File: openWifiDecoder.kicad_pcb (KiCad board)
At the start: 4 copper layers, 16 x 23.6 mm, 63 parts, among them IC1 DRV8212DRLR, J1 Motor, J24 Hall, U1 MIC5317-1.8xM5, U2 MIC5219-3.3YM5, U3 ESP32-S3-MINI-1, U4 ICM-20948, U5 LTC4054ES5-4.2, U6 TL331, U7 BQ27441DRZT-G1A

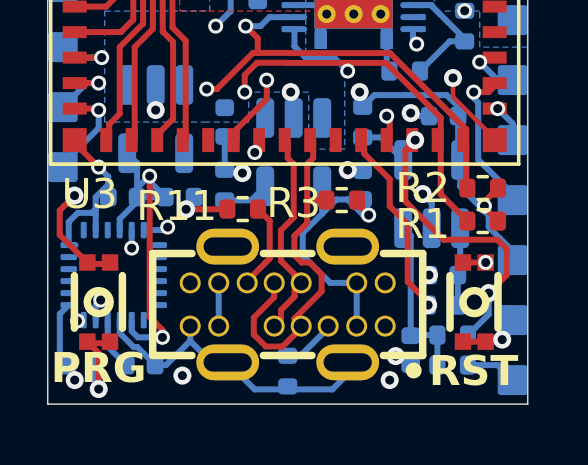
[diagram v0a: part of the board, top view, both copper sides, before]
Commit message: add EN PullUp
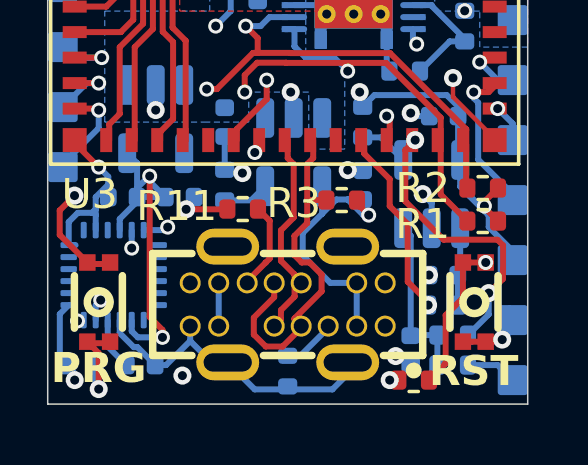
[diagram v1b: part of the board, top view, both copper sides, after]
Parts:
- added R14: 10k, Resistor_SMD:R_0402_1005Metric, F.Cu at (106.7, 86.8)
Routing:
- net Net-(U3-EN): track 18.6 -> 23.0 mm
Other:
- board text added: "1.1"
- board text removed: "1.0"

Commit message: finished Layout, started PCB design agound ESP32
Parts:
- added C16: 10u, Capacitor_SMD:C_0805_2012Metric, F.Cu at (113.9, 81.4)
- added C17: 10u X7R, Capacitor_SMD:C_0805_2012Metric, F.Cu at (113.9, 84.4)
- added C18: 1uF X7R, Capacitor_SMD:C_0402_1005Metric, F.Cu at (172.2, 73.8)
- added C19: 10u X7R, Capacitor_SMD:C_0805_2012Metric, F.Cu at (186.1, 91.9)
- added C20: .1uF X7R, Capacitor_SMD:C_0402_1005Metric, F.Cu at (176.1, 101.6)
- added C21: .1uF X7R, Capacitor_SMD:C_0402_1005Metric, F.Cu at (178.9, 97.6)
- added C22: .1uF X7R, Capacitor_SMD:C_0402_1005Metric, F.Cu at (161.2, 77.6)
- added C23: TBCC, Capacitor_SMD:C_0805_2012Metric, F.Cu at (166.9, 66.1)
- added C24: C, Capacitor_SMD:C_0402_1005Metric, F.Cu at (157.1, 67.0)
- added C25: C, Capacitor_SMD:C_0402_1005Metric, F.Cu at (157.0, 64.0)
- added C26: C, Capacitor_SMD:C_0402_1005Metric, F.Cu at (125.3, 83.2)
- added C27: C, Capacitor_SMD:C_0402_1005Metric, F.Cu at (125.3, 85.2)
- added L1: 1.5u 1.5A, Inductor_SMD:L_1008_2520Metric, F.Cu at (107.6, 72.9)
- added L2: 2n, Inductor_SMD:L_0402_1005Metric, F.Cu at (189.8, 88.4)
- added L3: 24n, Inductor_SMD:L_0402_1005Metric, F.Cu at (161.5, 66.7)
- added L4: L, Inductor_SMD:L_0402_1005Metric, F.Cu at (157.6, 65.5)
- added L5: L, Inductor_SMD:L_0402_1005Metric, F.Cu at (133.3, 78.0)
- added R15: 100k, Resistor_SMD:R_0603_1608Metric, F.Cu at (113.7, 87.2)
- added U8: W25Q16JVUUIQ, EasyEda:USON-8_L4.0-W3.0-P0.80-BL_AT25SL321, F.Cu at (164.0, 77.2)
- added U9: RFANT3216120A5T, EasyEda:FILTER-SMD_1206-2P-L3.2-W1.6-L, F.Cu at (159.1, 60.5)
- added Y1: 40MHz 10pF, Crystal:Crystal_SMD_2016-4Pin_2.0x1.6mm, F.Cu at (164.2, 66.0)
- BAT1, C1, C10, C11, C12, C13, C14, C15, C3, C4, C6, C7, C8, C9, IC1, IO1, IO10, IO11, IO12, IO13, IO14, IO15, IO16, IO17, IO18, IO19, IO2, IO3, IO4, IO5, IO6, IO7, IO8, IO9, J1, J24, R10, R12, R13, R4, R5, R6, R7, R8, R9, RX0, TX0, U1, U4, U5, U6, U7: moved to F.Cu
- C2: value 22uF X7R -> TBC; moved to F.Cu
- C5: value 1uF X7R -> 10u X7R; footprint Capacitor_SMD:C_0402_1005Metric -> Capacitor_SMD:C_0805_2012Metric; moved to F.Cu
- U2: value MIC5219-3.3YM5 -> TPS63051RMWR; footprint Package_TO_SOT_SMD:SOT-23-5 -> EasyEda:QFN-12_L2.5-W2.5-P0.50-TL; moved to F.Cu
- U3: value ESP32-S3-MINI-1 -> ESP32-S3; footprint RF_Module:ESP32-S2-MINI-1 -> Package_DFN_QFN:QFN-56-1EP_7x7mm_P0.4mm_EP4x4mm_ThermalVias
- moved C1 76.8 mm to (174.6, 83.5)
- moved C2 65.0 mm to (164.2, 68.8)
- moved U3 56.8 mm to (159.1, 72.3), turned to -45 degrees
- moved U2 30.1 mm to (115.3, 97.8), turned to 0 degrees
- moved C6 28.1 mm to (91.2, 91.8)
- moved J1 24.0 mm to (108.5, 93.8), turned to 0 degrees
- moved C10 23.8 mm to (94.1, 91.8), turned to 0 degrees
- moved IO12 23.4 mm to (101.5, 87.9), turned to 0 degrees
- moved IC1 22.8 mm to (112.2, 92.3)
- moved IO11 21.4 mm to (101.5, 85.9), turned to 0 degrees
- moved R5 20.3 mm to (91.2, 85.8), turned to 0 degrees
- moved R4 20.1 mm to (91.2, 83.9), turned to 0 degrees
- moved FLASH1 19.9 mm to (112.2, 72.4), turned to 0 degrees
- moved IO10 19.6 mm to (101.5, 83.9), turned to 0 degrees
- moved IO6 18.7 mm to (99.5, 87.9), turned to 0 degrees
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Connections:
- C1 pad 1: +3V3 -> Net-(C1-Pad1)
- C13 pad 2: +3V3 -> VDD_SPI
- C2 pad 1: +3V3 -> Net-(C2-Pad1)
- C5 pad 1: +3V3 -> VDD_SPI
- C8 pad 2: +3V3 -> VDD_SPI
- FLASH1 pad 3: Net-(U3-IO0) -> Net-(FLASH1-Pad3)
- FLASH1 pad 4: Net-(U3-IO0) -> Net-(FLASH1-Pad3)
- IO1 pad 1: Net-(IO1-Pin_1) -> unconnected-(IO1-Pin_1-Pad1)
- IO10 pad 1: Net-(IO10-Pin_1) -> unconnected-(IO10-Pin_1-Pad1)
- IO11 pad 1: Net-(IO11-Pin_1) -> unconnected-(IO11-Pin_1-Pad1)
- IO12 pad 1: Net-(IO12-Pin_1) -> unconnected-(IO12-Pin_1-Pad1)
- IO13 pad 1: Net-(IO13-Pin_1) -> unconnected-(IO13-Pin_1-Pad1)
- IO14 pad 1: Net-(IO14-Pin_1) -> unconnected-(IO14-Pin_1-Pad1)
- IO15 pad 1: Net-(IO15-Pin_1) -> unconnected-(IO15-Pin_1-Pad1)
- IO16 pad 1: Net-(IO16-Pin_1) -> unconnected-(IO16-Pin_1-Pad1)
- IO17 pad 1: Net-(IO17-Pin_1) -> unconnected-(IO17-Pin_1-Pad1)
- IO18 pad 1: Net-(IO18-Pin_1) -> unconnected-(IO18-Pin_1-Pad1)
- IO19 pad 1: Net-(IO19-Pin_1) -> unconnected-(IO19-Pin_1-Pad1)
- IO2 pad 1: Net-(IO2-Pin_1) -> unconnected-(IO2-Pin_1-Pad1)
- IO3 pad 1: Net-(IO3-Pin_1) -> unconnected-(IO3-Pin_1-Pad1)
- IO4 pad 1: Net-(IO4-Pin_1) -> unconnected-(IO4-Pin_1-Pad1)
- IO5 pad 1: Net-(IO5-Pin_1) -> unconnected-(IO5-Pin_1-Pad1)
- IO6 pad 1: Net-(IO6-Pin_1) -> unconnected-(IO6-Pin_1-Pad1)
- IO7 pad 1: Net-(IO7-Pin_1) -> unconnected-(IO7-Pin_1-Pad1)
- IO8 pad 1: Net-(IO8-Pin_1) -> unconnected-(IO8-Pin_1-Pad1)
- IO9 pad 1: Net-(IO9-Pin_1) -> unconnected-(IO9-Pin_1-Pad1)
- J24 pad 1: +3V3 -> VDD_SPI
- R1 pad 1: +3V3 -> VDD_SPI
- R10 pad 2: +3V3 -> VDD_SPI
- R14 pad 1: Net-(U3-EN) -> Net-(R14-Pad1)
- R14 pad 2: +3V3 -> VDD_SPI
- R2 pad 1: +3V3 -> VDD_SPI
- RESET1 pad 3: Net-(U3-EN) -> Net-(R14-Pad1)
- RESET1 pad 4: Net-(U3-EN) -> Net-(R14-Pad1)
- U2 pad 1: +BATT -> Net-(U2-L1)
- U2 pad 3: +BATT -> Net-(U2-L2)
- U2 pad 4: unconnected-(U2-BP-Pad4) -> VDD_SPI
- U2 pad 5: +3V3 -> VDD_SPI
- U3 pad 1: GND -> Net-(U3-LNA_IN)
- U3 pad 10: Net-(IO4-Pin_1) -> /ESP/GPIO5
- U3 pad 11: Net-(IO9-Pin_1) -> /ESP/GPIO6
- U3 pad 12: Net-(IO10-Pin_1) -> /ESP/GPIO7
- U3 pad 13: Net-(IO3-Pin_1) -> /ESP/GPIO8
- U3 pad 14: Net-(IO2-Pin_1) -> /ESP/GPIO9
- U3 pad 15: Net-(IO1-Pin_1) -> /ESP/GPIO10
- U3 pad 16: Net-(IO11-Pin_1) -> /ESP/GPIO11
- U3 pad 17: Net-(IO12-Pin_1) -> /ESP/GPIO12
- U3 pad 18: Net-(IO13-Pin_1) -> /ESP/GPIO13
- U3 pad 19: Net-(IO14-Pin_1) -> /ESP/GPIO14
- U3 pad 2: GND -> Net-(L2-Pad2)
- U3 pad 20: unconnected-(U3-IO16-Pad20) -> VDD_SPI
- U3 pad 21: IMU_INT -> unconnected-(U3-XTAL_32K_P-Pad21)
- U3 pad 22: FSYNC -> unconnected-(U3-XTAL_32K_N-Pad22)
- U3 pad 23: D- -> /ESP/GPIO17
- U3 pad 24: D+ -> /ESP/GPIO18
- U3 pad 25: unconnected-(U3-IO21-Pad25) -> /ESP/GPIO19
- U3 pad 26: COMP_DAC -> /ESP/GPIO20
- U3 pad 27: GAUGE_INT -> /ESP/GPIO21
- U3 pad 28: DIG_HALL -> unconnected-(U3-SPICS1-Pad28)
- U3 pad 29: SDA -> VDD_SPI
- U3 pad 3: +3V3 -> Net-(L2-Pad2)
- U3 pad 30: SCL -> HOLD
- U3 pad 31: Net-(IO18-Pin_1) -> WP
- U3 pad 32: Net-(IO19-Pin_1) -> CS
- U3 pad 33: Net-(IO17-Pin_1) -> CLK
- U3 pad 34: unconnected-(U3-IO38-Pad34) -> SDO
- U3 pad 35: unconnected-(U3-IO39-Pad35) -> SDI
- U3 pad 36: Net-(IO16-Pin_1) -> unconnected-(U3-SPICLK_N-Pad36)
- U3 pad 37: MPWM1 -> unconnected-(U3-SPICLK_P-Pad37)
- U3 pad 38: MPWM2 -> /ESP/GPIO33
- U3 pad 39: TX -> /ESP/GPIO34
- U3 pad 4: Net-(U3-IO0) -> VDD_SPI
- U3 pad 40: RX -> /ESP/GPIO35
- U3 pad 41: Net-(IO15-Pin_1) -> /ESP/GPIO36
- U3 pad 42: GND -> /ESP/GPIO37
- U3 pad 43: GND -> /ESP/GPIO38
- U3 pad 45: Net-(U3-EN) -> unconnected-(U3-MTDO-Pad45)
- U3 pad 46: GND -> VDD_SPI
- U3 pad 47: GND -> unconnected-(U3-MTDI-Pad47)
- U3 pad 48: GND -> unconnected-(U3-MTMS-Pad48)
- U3 pad 49: GND -> unconnected-(U3-U0TXD-Pad49)
- U3 pad 5: Net-(IO8-Pin_1) -> /ESP/GPIO0
- U3 pad 50: GND -> unconnected-(U3-U0RXD-Pad50)
- U3 pad 51: GND -> unconnected-(U3-GPIO45-Pad51)
- U3 pad 52: GND -> unconnected-(U3-GPIO46-Pad52)
- U3 pad 53: GND -> Net-(U3-XTAL_N)
- U3 pad 54: GND -> Net-(U3-XTAL_P)
- U3 pad 55: GND -> VDD_SPI
- U3 pad 56: GND -> VDD_SPI
- U3 pad 6: Net-(IO7-Pin_1) -> /ESP/GPIO1
- U3 pad 7: Net-(IO6-Pin_1) -> /ESP/GPIO2
- U3 pad 8: Net-(IO5-Pin_1) -> /ESP/GPIO3
- U3 pad 9: unconnected-(U3-IO5-Pad9) -> /ESP/GPIO4
- U4 pad 13: +3V3 -> VDD_SPI
- U6 pad 5: +3V3 -> VDD_SPI
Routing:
- net GND: track 35.6 -> 0.00 mm, vias 31 -> 0
- net +3V3: track 33.6 -> 0.00 mm, vias 8 -> 0
- net Net-(U3-EN): track 23.0 -> 0.00 mm, vias 2 -> 0
- net SCL: track 21.5 -> 0.00 mm, vias 3 -> 0
- net SDA: track 21.3 -> 0.00 mm, vias 3 -> 0
- net Net-(IO14-Pin_1): track 20.0 -> 0.00 mm, vias 1 -> 0
- net Net-(IO13-Pin_1): track 18.7 -> 0.00 mm, vias 1 -> 0
- net Net-(IO11-Pin_1): track 17.9 -> 0.00 mm, vias 1 -> 0
- net Net-(IO12-Pin_1): track 17.9 -> 0.00 mm, vias 1 -> 0
- net Net-(U3-IO0): track 16.8 -> 0.00 mm, vias 2 -> 0
- net +5V: track 16.2 -> 0.00 mm, vias 1 -> 0
- net IMU_INT: track 15.8 -> 0.00 mm, vias 2 -> 0
- net Net-(BAT1-Pin_2): track 14.2 -> 0.00 mm, vias 2 -> 0
- net Net-(IO16-Pin_1): track 14.2 -> 0.00 mm, vias 1 -> 0
- net Net-(IO10-Pin_1): track 12.8 -> 0.00 mm, vias 1 -> 0
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- removed copper zone on In1.Cu, net +3V3
- removed copper zone on B.Cu, net +BATT
- removed copper zone on F.Cu, net GND
- removed copper zone on In2.Cu, net GND
- removed copper zone on B.Cu, net Net-(BAT1-Pin_2)
- removed copper zone on B.Cu, net Net-(IC1-OUT1)
- removed copper zone on B.Cu, net Net-(IC1-OUT2)
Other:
- board outline removed
- board text removed: "+"
- board text removed: "-"
- board text removed: "1"
- board text removed: "1.1"
- board text removed: "10"
- board text removed: "11"
- board text removed: "12"
- board text removed: "13"
- board text removed: "14"
- board text removed: "15"
- board text removed: "16"
- board text removed: "17"
- board text removed: "18"
- board text removed: "19"
- board text removed: "2"
- board text removed: "3"
- board text removed: "4"
- board text removed: "5"
- board text removed: "6"
- board text removed: "7"
- board text removed: "8"
- board text removed: "9"
- board text removed: "BAT"
- board text removed: "HALL"
- board text removed: "Motor"
- board text removed: "PRG"
- board text removed: "R"
- board text removed: "RST"
- board text removed: "T"
- board text removed: "der Graph"
- board text removed: "openWiFi decoder"

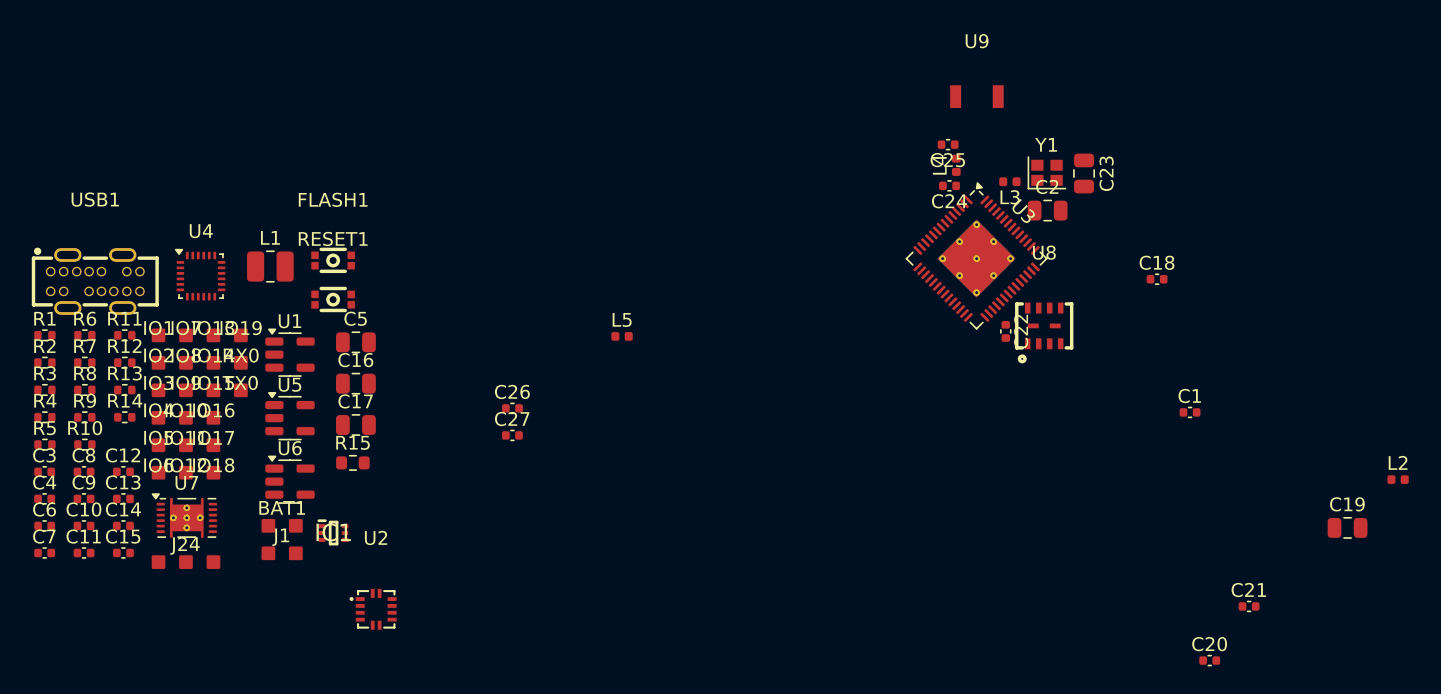
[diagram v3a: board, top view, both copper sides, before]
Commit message: pcb parts placed not connected
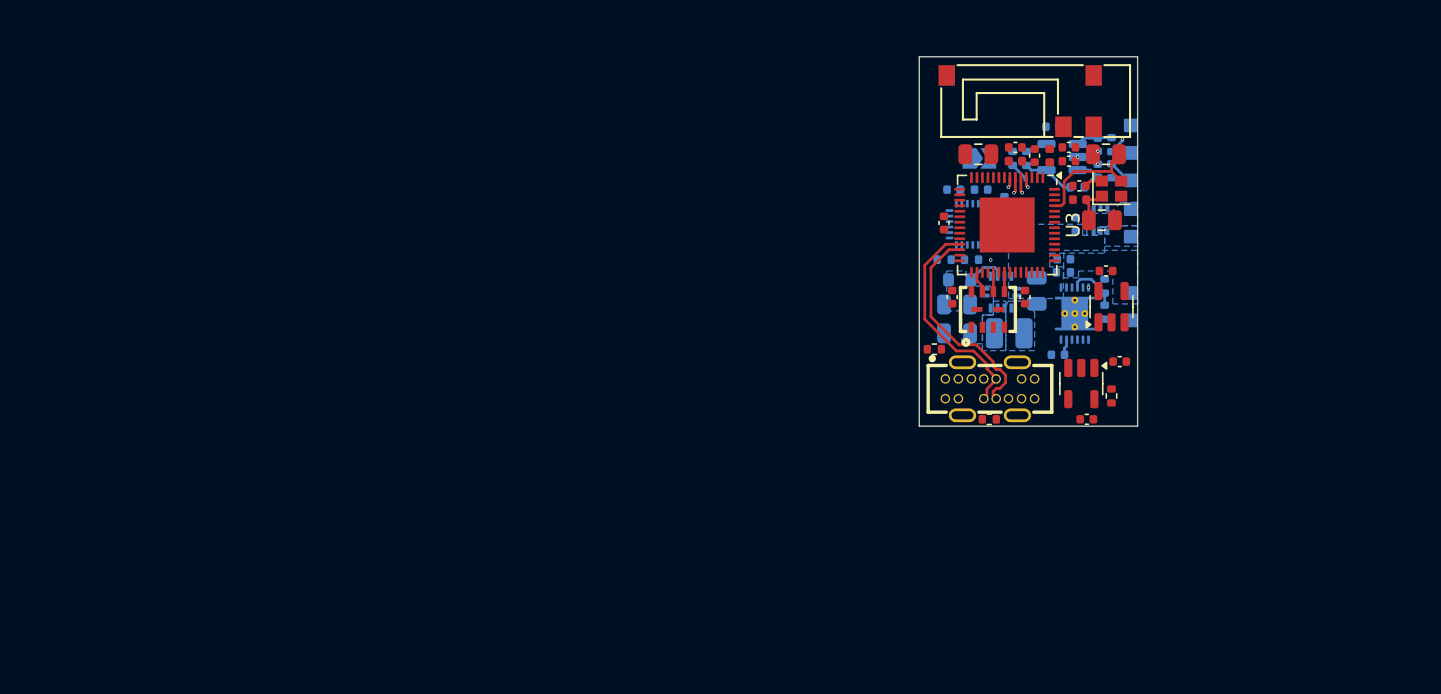
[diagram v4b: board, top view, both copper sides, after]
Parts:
- removed C27: C, Capacitor_SMD:C_0402_1005Metric
- removed FLASH1: FLASH, easyeda2kicad:SW-SMD_4P-L2.6-W1.6-P0.75-LS3.0
- removed IO1, IO8: 1, padLib:SolderPad_1mm_1Pin
- removed IO10, IO11, IO12, IO13, IO14, IO15, IO16, IO17, IO18, IO19, IO4, IO5, IO6, IO9, RX0, TX0: Conn_01x01_Socket, padLib:SolderPad_1mm_1Pin
- removed IO2, IO7: 2, padLib:SolderPad_1mm_1Pin
- removed IO3: 3, padLib:SolderPad_1mm_1Pin
- removed L5: L, Inductor_SMD:L_0402_1005Metric
- removed R3: USB_PU, Resistor_SMD:R_0402_1005Metric
- removed RESET1: RESET, easyeda2kicad:SW-SMD_4P-L2.6-W1.6-P0.75-LS3.0
- removed U9: RFANT3216120A5T, EasyEda:FILTER-SMD_1206-2P-L3.2-W1.6-L
- added ANT1: PRO-OB-440, EasyEda:ANT-SMD_5P-L13.8-W5.2_PRO-OB-440, F.Cu at (162.2, 60.8)
- added JP1: Download Mode, padLib:SolderJumper-2_P1.3mm_Open_TrianglePad1.0x1.5mm_SMALLER, B.Cu at (159.3, 65.0)
- BAT1, C10, C11, C13, C14, C15, C16, C17, C5, C6, C7, C8, C9, IC1, J1, J24, L1, R1, R10, R12, R13, R14, R15, R2, R4, R5, R6, R8, U2, U4, U6, U7: moved to B.Cu
- C26: value C -> 1uF X7R
- U3: footprint Package_DFN_QFN:QFN-56-1EP_7x7mm_P0.4mm_EP4x4mm_ThermalVias -> Package_DFN_QFN:QFN-56-1EP_7x7mm_P0.4mm_EP4x4mm
- moved C4 79.1 mm to (168.5, 73.2)
- moved C3 78.7 mm to (169.5, 79.8), turned to 180 degrees
- moved C6 78.2 mm to (166.3, 69.8), turned to -90 degrees
- moved R5 77.8 mm to (168.4, 76.2), turned to 90 degrees
- moved C15 76.9 mm to (167.9, 64.0), turned to -90 degrees
- moved C14 75.5 mm to (167.9, 65.9), turned to -90 degrees
- moved J24 75.0 mm to (170.3, 64.6), turned to -90 degrees
- moved R4 74.9 mm to (165.4, 73.3), turned to 180 degrees
- moved R7 74.8 mm to (168.9, 82.3), turned to -90 degrees
- moved R6 74.4 mm to (168.4, 74.3), turned to 90 degrees
- moved R13 74.0 mm to (168.9, 64.0), turned to 90 degrees
- moved C10 73.9 mm to (165.4, 72.3), turned to 180 degrees
- moved R8 73.8 mm to (166.4, 67.1), turned to 180 degrees
- moved R12 73.2 mm to (168.9, 65.9), turned to 90 degrees
- moved C13 72.9 mm to (164.6, 62.7), turned to 180 degrees
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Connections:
- net /ESP/GPIO3 renamed /ESP/GPIO3 JTAG Source
- C1 pad 1: Net-(C1-Pad1) -> +3V3
- C13 pad 2: VDD_SPI -> +3V3
- C16 pad 1: VDD_SPI -> +3V3
- C19 pad 1: VDD_SPI -> +3V3
- C20 pad 2: VDD_SPI -> +3V3
- C21 pad 2: VDD_SPI -> +3V3
- C22 pad 1: VDD_SPI -> Net-(U3-VDD3P3_CPU)
- C25 pad 1: Net-(C25-Pad1) -> Net-(ANT1-FEED)
- C26 pad 1: Net-(C25-Pad1) -> GND
- C26 pad 2: GND -> Net-(C26-Pad2)
- C3 pad 1: +BATT -> +3V3
- C5 pad 1: VDD_SPI -> +3V3
- C8 pad 2: VDD_SPI -> +3V3
- J24 pad 1: VDD_SPI -> +3V3
- L2 pad 1: Net-(C1-Pad1) -> +3V3
- L2 pad 2: Net-(L2-Pad2) -> Net-(C26-Pad2)
- L4 pad 2: Net-(C25-Pad1) -> Net-(ANT1-FEED)
- R1 pad 1: VDD_SPI -> +3V3
- R10 pad 2: VDD_SPI -> +3V3
- R14 pad 1: Net-(R14-Pad1) -> /ESP/RST
- R14 pad 2: VDD_SPI -> +3V3
- R15 pad 1: VDD_SPI -> +3V3
- R2 pad 1: VDD_SPI -> +3V3
- U1 pad 1: +BATT -> +3V3
- U1 pad 3: +BATT -> +3V3
- U2 pad 4: VDD_SPI -> +3V3
- U2 pad 5: VDD_SPI -> +3V3
- U3 pad 10: /ESP/GPIO5 -> MPWM1
- U3 pad 11: /ESP/GPIO6 -> IMU_INT
- U3 pad 2: Net-(L2-Pad2) -> Net-(C26-Pad2)
- U3 pad 20: VDD_SPI -> +3V3
- U3 pad 23: /ESP/GPIO17 -> SCL
- U3 pad 24: /ESP/GPIO18 -> SDA
- U3 pad 25: /ESP/GPIO19 -> D-
- U3 pad 26: /ESP/GPIO20 -> D+
- U3 pad 27: /ESP/GPIO21 -> FSYNC
- U3 pad 3: Net-(L2-Pad2) -> Net-(C26-Pad2)
- U3 pad 4: VDD_SPI -> /ESP/RST
- U3 pad 42: /ESP/GPIO37 -> GAUGE_INT
- U3 pad 46: VDD_SPI -> Net-(U3-VDD3P3_CPU)
- U3 pad 5: /ESP/GPIO0 -> /ESP/GPIO0 Flash Mode
- U3 pad 51: unconnected-(U3-GPIO45-Pad51) -> GND
- U3 pad 52: unconnected-(U3-GPIO46-Pad52) -> GND
- U3 pad 55: VDD_SPI -> +3V3
- U3 pad 56: VDD_SPI -> +3V3
- U3 pad 6: /ESP/GPIO1 -> COMP_DAC
- U3 pad 7: /ESP/GPIO2 -> DIG_HALL
- U3 pad 9: /ESP/GPIO4 -> MPWM2
- U4 pad 13: VDD_SPI -> +3V3
- U6 pad 5: VDD_SPI -> +3V3
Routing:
- net D-: track 0.00 -> 16.0 mm
- net D+: track 0.00 -> 15.9 mm
- net Net-(U3-XTAL_N): track 0.00 -> 8.57 mm
- net DIG_HALL: track 0.00 -> 4.60 mm, vias 0 -> 1
- net Net-(U6-+): track 0.00 -> 3.98 mm
- net Net-(U7-BIN): track 0.00 -> 3.77 mm
- net Net-(C2-Pad1): track 0.00 -> 2.97 mm
- net Net-(U2-PG): track 0.00 -> 2.81 mm
- net Net-(U6--): track 0.00 -> 2.65 mm
- net COMP_DAC: track 0.00 -> 2.38 mm, vias 0 -> 2
- net /ESP/RST: track 0.00 -> 2.19 mm, vias 0 -> 1
- net Net-(J24-Pin_3): track 0.00 -> 1.90 mm
- net HOLD: track 0.00 -> 1.57 mm
- net SDI: track 0.00 -> 1.40 mm
- net CLK: track 0.00 -> 1.40 mm
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- added copper zone on B.Cu, net +3V3
- added copper zone on B.Cu, net +BATT
- added copper zone on B.Cu, net Net-(BAT1-Pin_2)
- added copper zone on B.Cu, net Net-(IC1-OUT1)
- added copper zone on B.Cu, net Net-(IC1-OUT2)
- added copper zone on B.Cu, net Net-(U2-L1)
- added copper zone on B.Cu, net Net-(U2-L2)
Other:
- board outline added: 15.9 x 26.9 mm

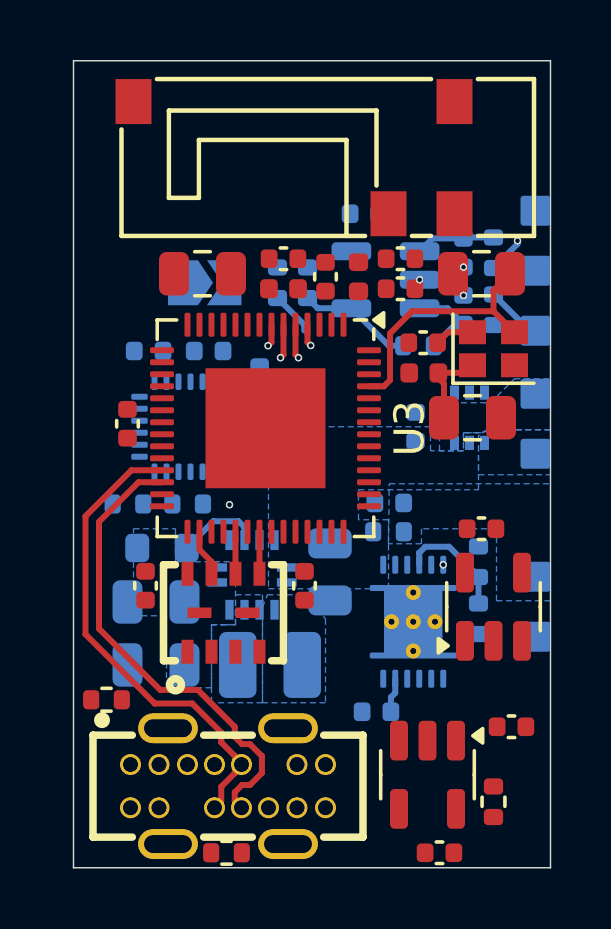
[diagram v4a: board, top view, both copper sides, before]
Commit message: pcb complete, drc failing 133 Errors
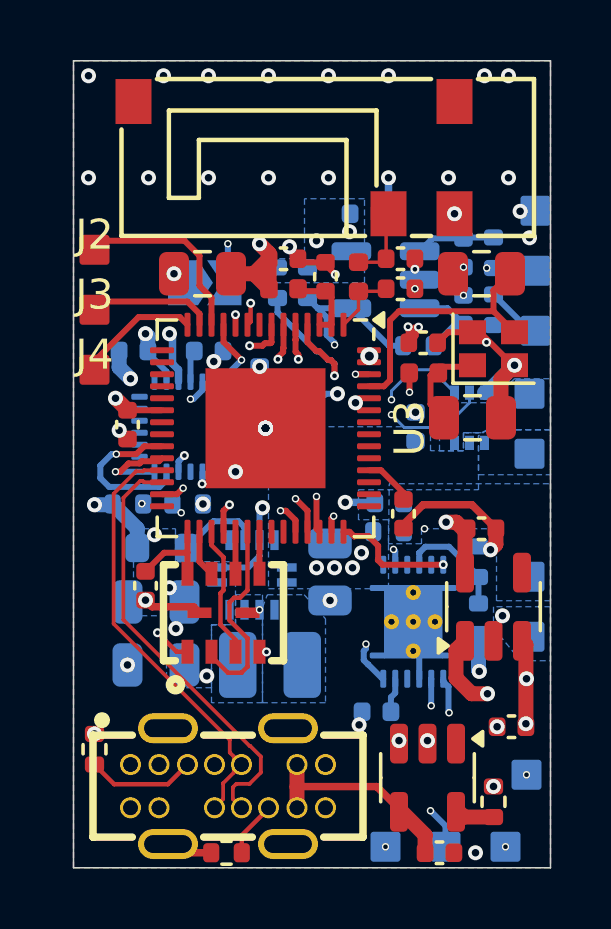
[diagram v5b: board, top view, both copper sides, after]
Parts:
- added J2: Conn_01x01_Pin, padLib:SolderPad_1mm_1Pin, F.Cu at (155.6, 63.9)
- added J3: Conn_01x01_Pin, padLib:SolderPad_1mm_1Pin, F.Cu at (155.6, 65.9)
- added J4: Conn_01x01_Pin, padLib:SolderPad_1mm_1Pin, F.Cu at (155.6, 67.9)
- added J5: Conn_01x01_Pin, padLib:SolderPad_1mm_1Pin, B.Cu at (165.3, 83.8)
- added J6: Conn_01x01_Pin, padLib:SolderPad_1mm_1Pin, B.Cu at (167.3, 83.8)
- added J7: Conn_01x01_Pin, padLib:SolderPad_1mm_1Pin, B.Cu at (169.3, 83.8)
- added J8: Conn_01x01_Pin, padLib:SolderPad_1mm_1Pin, B.Cu at (170.0, 81.4)
- moved C22 4.08 mm to (165.9, 72.7)
- moved R9 1.70 mm to (155.6, 80.5), turned to 90 degrees
- moved C7 0.50 mm to (156.9, 67.3)
- moved BAT1 0.20 mm to (170.1, 75.8)
- moved J1 0.20 mm to (170.1, 69.7)
- moved U5 0.10 mm to (166.7, 81.5)
- turned R11 to 180 degrees
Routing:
- net GND: track 1.31 -> 26.5 mm, vias 3 -> 56
- net SCL: track 0.00 -> 20.7 mm, vias 0 -> 3
- net SDA: track 0.00 -> 19.5 mm, vias 0 -> 3
- net +3V3: track 0.00 -> 19.1 mm, vias 0 -> 18
- net +1V8: track 0.00 -> 19.1 mm, vias 0 -> 3
- net /ESP/GPIO35: track 0.00 -> 17.6 mm, vias 0 -> 2
- net MPWM2: track 0.00 -> 15.7 mm, vias 0 -> 2
- net /ESP/GPIO34: track 0.00 -> 15.5 mm, vias 0 -> 2
- net +5V: track 0.00 -> 14.5 mm
- net /ESP/GPIO36: track 0.00 -> 14.4 mm, vias 0 -> 2
- net /ESP/GPIO33: track 0.00 -> 13.9 mm, vias 0 -> 2
- net MPWM1: track 0.00 -> 12.8 mm, vias 0 -> 2
- net /ESP/GPIO0 Flash Mode: track 1.14 -> 11.2 mm, vias 1 -> 2
- net COMP_DAC: track 2.38 -> 11.4 mm
- net CS: track 0.00 -> 7.50 mm, vias 1 -> 2
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- added copper zone on In3.Cu, net +3V3
- added copper zone on In3.Cu, net +BATT
- added copper zone on B.Cu, net GND
- added copper zone on F.Cu, net GND
- added copper zone on In1.Cu, net GND
- added copper zone on In4.Cu, net GND
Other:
- copper layers 4 -> 6
